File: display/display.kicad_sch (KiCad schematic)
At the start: 14 parts, among them J1 DIN41612_03x32_ABC

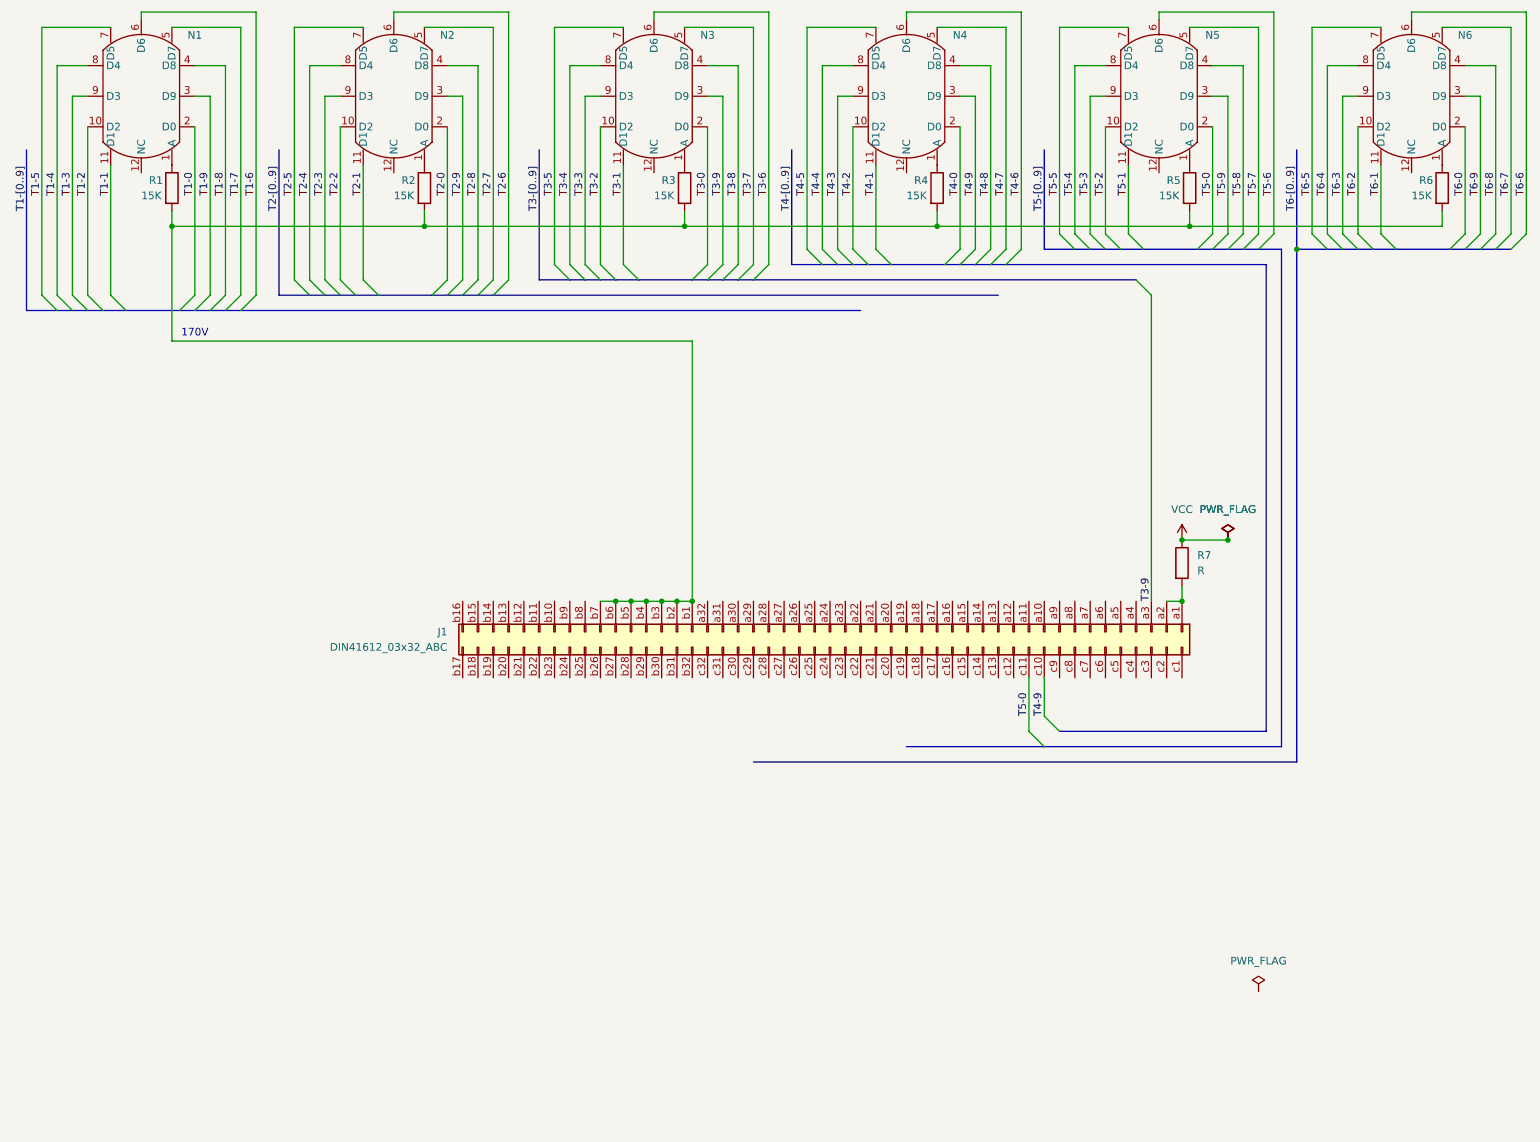
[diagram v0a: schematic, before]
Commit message: Complete rev 1 (alpha) schematics. Both pass DRC.
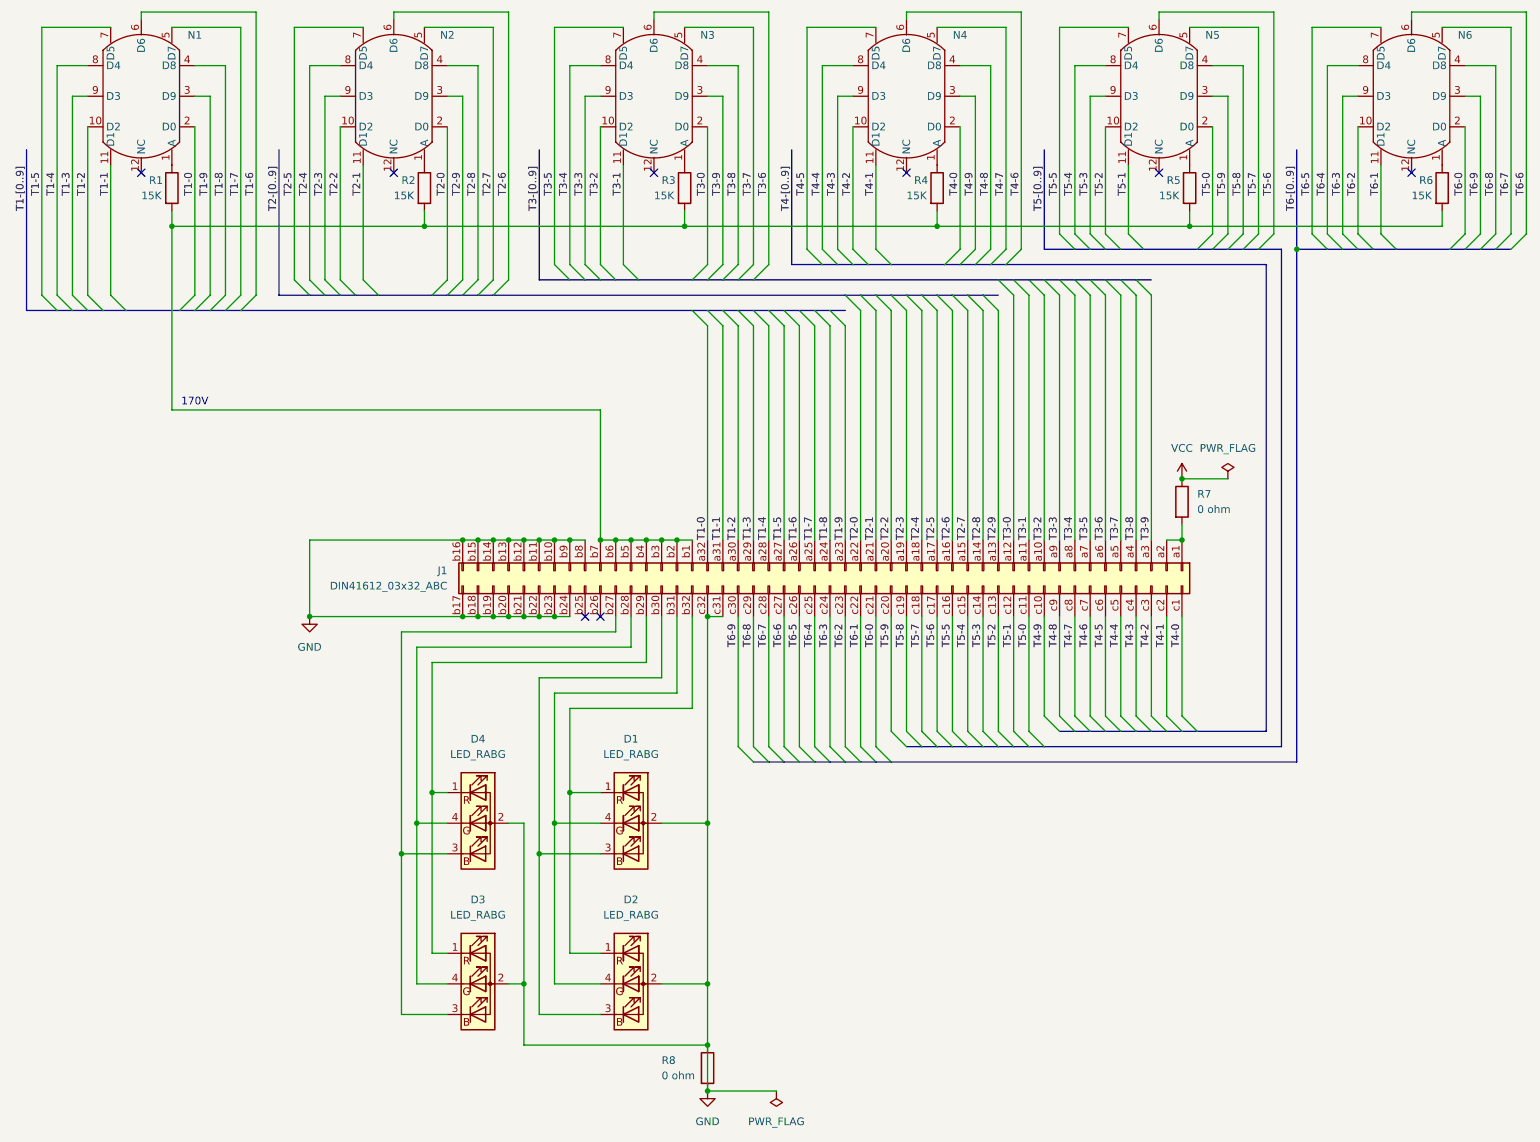
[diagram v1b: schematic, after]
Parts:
- added D1, D2, D3, D4: LED_RABG, symbol Device:LED_RABG
- added R8: 0 ohm, symbol Device:R
- R7: value R -> 0 ohm
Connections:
- net T1-0: now also J1.a32 (Pin_a32)
- net T1-1: now also J1.a31 (Pin_a31)
- net T1-2: now also J1.a30 (Pin_a30)
- net T1-3: now also J1.a29 (Pin_a29)
- net T1-4: now also J1.a28 (Pin_a28)
- net T1-5: now also J1.a27 (Pin_a27)
- net T1-6: now also J1.a26 (Pin_a26)
- net T1-7: now also J1.a25 (Pin_a25)
- net T1-8: now also J1.a24 (Pin_a24)
- net T1-9: now also J1.a23 (Pin_a23)
- net T2-0: now also J1.a22 (Pin_a22)
- net T2-1: now also J1.a21 (Pin_a21)
- net T2-2: now also J1.a20 (Pin_a20)
- net T2-3: now also J1.a19 (Pin_a19)
- net T2-4: now also J1.a18 (Pin_a18)
- net T2-5: now also J1.a17 (Pin_a17)
- net T2-6: now also J1.a16 (Pin_a16)
- net T2-7: now also J1.a15 (Pin_a15)
- net T2-8: now also J1.a14 (Pin_a14)
- net T2-9: now also J1.a13 (Pin_a13)
- net T3-0: now also J1.a12 (Pin_a12)
- net T3-1: now also J1.a11 (Pin_a11)
- net T3-2: now also J1.a10 (Pin_a10)
- net T3-3: now also J1.a9 (Pin_a9)
- net T3-4: now also J1.a8 (Pin_a8)
- net T3-5: now also J1.a7 (Pin_a7)
- net T3-6: now also J1.a6 (Pin_a6)
- net T3-7: now also J1.a5 (Pin_a5)
- net T3-8: now also J1.a4 (Pin_a4)
- net T4-0: now also J1.c1 (Pin_c1)
- net T4-1: now also J1.c2 (Pin_c2)
- net T4-2: now also J1.c3 (Pin_c3)
- net T4-3: now also J1.c4 (Pin_c4)
- net T4-4: now also J1.c5 (Pin_c5)
- net T4-5: now also J1.c6 (Pin_c6)
- net T4-6: now also J1.c7 (Pin_c7)
- net T4-7: now also J1.c8 (Pin_c8)
- net T4-8: now also J1.c9 (Pin_c9)
- net T5-1: now also J1.c12 (Pin_c12)
- net T5-2: now also J1.c13 (Pin_c13)
- net T5-3: now also J1.c14 (Pin_c14)
- net T5-4: now also J1.c15 (Pin_c15)
- net T5-5: now also J1.c16 (Pin_c16)
- net T5-6: now also J1.c17 (Pin_c17)
- net T5-7: now also J1.c18 (Pin_c18)
- net T5-8: now also J1.c19 (Pin_c19)
- net T5-9: now also J1.c20 (Pin_c20)
- net T6-0: now also J1.c21 (Pin_c21)
- net T6-1: now also J1.c22 (Pin_c22)
- net T6-2: now also J1.c23 (Pin_c23)
- net T6-3: now also J1.c24 (Pin_c24)
- net T6-4: now also J1.c25 (Pin_c25)
- net T6-5: now also J1.c26 (Pin_c26)
- net T6-6: now also J1.c27 (Pin_c27)
- net T6-7: now also J1.c28 (Pin_c28)
- net T6-8: now also J1.c29 (Pin_c29)
- net T6-9: now also J1.c30 (Pin_c30)
- net GND: now reaches J1.b10 (Pin_b10)
- net GND: now also J1.b11 (Pin_b11), J1.b12 (Pin_b12), J1.b13 (Pin_b13), J1.b14 (Pin_b14), J1.b15 (Pin_b15), J1.b16 (Pin_b16), J1.b17 (Pin_b17), J1.b18 (Pin_b18), J1.b19 (Pin_b19), J1.b20 (Pin_b20), J1.b21 (Pin_b21), J1.b22 (Pin_b22), J1.b23 (Pin_b23), J1.b24 (Pin_b24), J1.b8 (Pin_b8), J1.b9 (Pin_b9), J1.c31 (Pin_c31), J1.c32 (Pin_c32), D1.2 (A), D2.2 (A), D3.2 (A), D4.2 (A), R8.1, R8.2
- net at J1.b27 (Pin_b27): now also D3.3 (BK), D4.3 (BK)
- net at J1.b28 (Pin_b28): now also D3.4 (GK), D4.4 (GK)
- net at J1.b29 (Pin_b29): now also D3.1 (RK), D4.1 (RK)
- net at J1.b30 (Pin_b30): now also D1.3 (BK), D2.3 (BK)
- net at J1.b31 (Pin_b31): now also D1.4 (GK), D2.4 (GK)
- net at J1.b32 (Pin_b32): now also D1.1 (RK), D2.1 (RK)
- no-connect marks 0 -> 8
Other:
- moved on the sheet: J1, R7

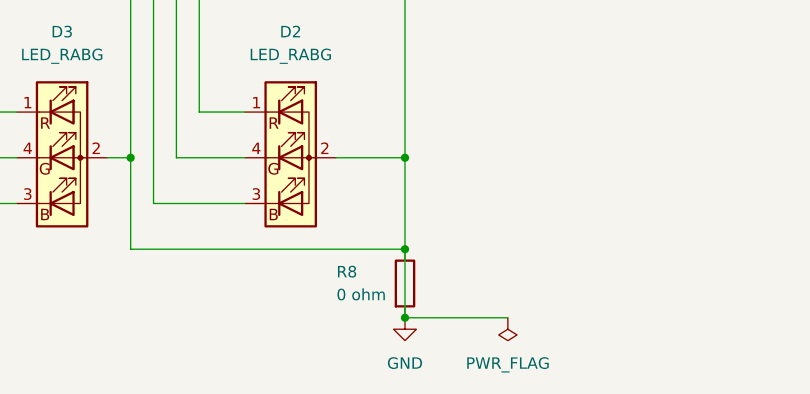
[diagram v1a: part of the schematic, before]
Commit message: Assign footprints for display and create PCB design
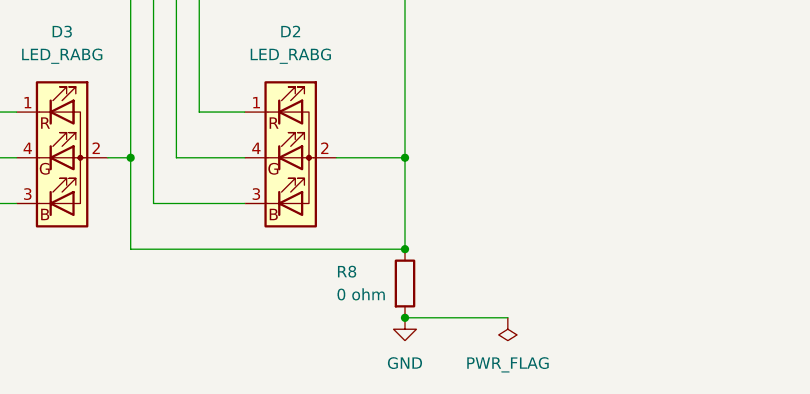
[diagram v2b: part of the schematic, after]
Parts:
- D1, D2, D3, D4: footprint (none) -> LED_THT:LED_D5.0mm-4_RGB
- J1: footprint (none) -> Connector_DIN:DIN41612_R_3x32_Female_Horizontal_THT
- N1, N2, N3, N4, N5, N6: footprint (none) -> hatsunearu:IN_12B_Socket
- R1, R2, R3, R4, R5, R6, R7, R8: footprint (none) -> Resistor_THT:R_Box_L14.0mm_W5.0mm_P9.00mm
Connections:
- net GND: no longer D1.2 (A), D2.2 (A), D3.2 (A), D4.2 (A), J1.c31 (Pin_c31), J1.c32 (Pin_c32), R8.1
- new net: D1.2 (A), D2.2 (A), D3.2 (A), D4.2 (A), J1.c31 (Pin_c31), J1.c32 (Pin_c32), R8.1
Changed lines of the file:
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@@
 		)
 	)
-	(wire
-		(pts
-			(xy 129.54 196.85) (xy 129.54 189.23)
-		)
-		(stroke
-			(width 0)
-			(type default)
-		)
-	)
 	(bus
 		(pts
@@
 			)
 		)
-		(property "Footprint" ""
+		(property "Footprint" "hatsunearu:IN_12B_Socket"
 			(at 246.38 31.75 0)
 			(effects
@@
 			)
 		)
-		(property "Footprint" ""
+		(property "Footprint" "hatsunearu:IN_12B_Socket"
 			(at 162.56 31.75 0)
 			(effects
@@
 			)
 		)
-		(property "Footprint" ""
+		(property "Footprint" "Resistor_THT:R_Box_L14.0mm_W5.0mm_P9.00mm"
 			(at 165.862 46.99 90)
 			(effects
@@
 			)
 		)
-		(property "Footprint" ""
+		(property "Footprint" "Connector_DIN:DIN41612_R_3x32_Female_Horizontal_THT"
 			(at 170.18 110.49 0)
 			(effects
@@
 			)
 		)
-		(property "Footprint" ""
+		(property "Footprint" "Resistor_THT:R_Box_L14.0mm_W5.0mm_P9.00mm"
 			(at 206.502 99.06 90)
 			(effects
@@
 			)
 		)
-		(property "Footprint" ""
+		(property "Footprint" "LED_THT:LED_D5.0mm-4_RGB"
 			(at 91.44 153.67 0)
 			(effects
@@
 			)
 		)
-		(property "Footprint" ""
+		(property "Footprint" "Resistor_THT:R_Box_L14.0mm_W5.0mm_P9.00mm"
 			(at 123.952 46.99 90)
 			(effects
@@
 			)
 		)
-		(property "Footprint" ""
+		(property "Footprint" "Resistor_THT:R_Box_L14.0mm_W5.0mm_P9.00mm"
 			(at 38.862 46.99 90)
 			(effects
@@
 			)
 		)
-		(property "Footprint" ""
+		(property "Footprint" "Resistor_THT:R_Box_L14.0mm_W5.0mm_P9.00mm"
 			(at 207.772 46.99 90)
 			(effects
@@
 			)
 		)
-		(property "Footprint" ""
+		(property "Footprint" "LED_THT:LED_D5.0mm-4_RGB"
 			(at 116.84 180.34 0)
 			(effects
@@
 			)
 		)
-		(property "Footprint" ""
+		(property "Footprint" "Resistor_THT:R_Box_L14.0mm_W5.0mm_P9.00mm"
 			(at 127.762 193.04 90)
 			(effects
@@
 			)
 		)
-		(property "Footprint" ""
+		(property "Footprint" "hatsunearu:IN_12B_Socket"
 			(at 77.47 31.75 0)
 			(effects
@@
 			)
 		)
-		(property "Footprint" ""
+		(property "Footprint" "hatsunearu:IN_12B_Socket"
 			(at 35.56 31.75 0)
 			(effects
@@
 			)
 		)
-		(property "Footprint" ""
+		(property "Footprint" "hatsunearu:IN_12B_Socket"
 			(at 120.65 31.75 0)
 			(effects
@@
 			)
 		)
-		(property "Footprint" ""
+		(property "Footprint" "LED_THT:LED_D5.0mm-4_RGB"
 			(at 116.84 153.67 0)
 			(effects
@@
 			)
 		)
-		(property "Footprint" ""
+		(property "Footprint" "Resistor_THT:R_Box_L14.0mm_W5.0mm_P9.00mm"
 			(at 80.772 46.99 90)
 			(effects
@@
 			)
 		)
-		(property "Footprint" ""
+		(property "Footprint" "LED_THT:LED_D5.0mm-4_RGB"
 			(at 91.44 180.34 0)
 			(effects
@@
 			)
 		)
-		(property "Footprint" ""
+		(property "Footprint" "Resistor_THT:R_Box_L14.0mm_W5.0mm_P9.00mm"
 			(at 249.682 46.99 90)
 			(effects
@@
 			)
 		)
-		(property "Footprint" ""
+		(property "Footprint" "hatsunearu:IN_12B_Socket"
 			(at 204.47 31.75 0)
 			(effects

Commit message: Layout is ongoing
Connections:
- net T4-0: now also J1.c30 (Pin_c30); no longer J1.c1 (Pin_c1)
- net T4-1: now also J1.c29 (Pin_c29); no longer J1.c2 (Pin_c2)
- net T4-2: now also J1.c28 (Pin_c28); no longer J1.c3 (Pin_c3)
- net T4-3: now also J1.c27 (Pin_c27); no longer J1.c4 (Pin_c4)
- net T4-4: now also J1.c26 (Pin_c26); no longer J1.c5 (Pin_c5)
- net T4-5: now also J1.c25 (Pin_c25); no longer J1.c6 (Pin_c6)
- net T4-6: now also J1.c24 (Pin_c24); no longer J1.c7 (Pin_c7)
- net T4-7: now also J1.c23 (Pin_c23); no longer J1.c8 (Pin_c8)
- net T4-8: now also J1.c22 (Pin_c22); no longer J1.c9 (Pin_c9)
- net T4-9: now also J1.c21 (Pin_c21); no longer J1.c10 (Pin_c10)
- net T5-0: now also J1.c20 (Pin_c20); no longer J1.c11 (Pin_c11)
- net T5-1: now also J1.c19 (Pin_c19); no longer J1.c12 (Pin_c12)
- net T5-2: now also J1.c18 (Pin_c18); no longer J1.c13 (Pin_c13)
- net T5-3: now also J1.c17 (Pin_c17); no longer J1.c14 (Pin_c14)
- net T5-4: now also J1.c16 (Pin_c16); no longer J1.c15 (Pin_c15)
- net T5-5: now also J1.c15 (Pin_c15); no longer J1.c16 (Pin_c16)
- net T5-6: now also J1.c14 (Pin_c14); no longer J1.c17 (Pin_c17)
- net T5-7: now also J1.c13 (Pin_c13); no longer J1.c18 (Pin_c18)
- net T5-8: now also J1.c12 (Pin_c12); no longer J1.c19 (Pin_c19)
- net T5-9: now also J1.c11 (Pin_c11); no longer J1.c20 (Pin_c20)
- net T6-0: now also J1.c5 (Pin_c5); no longer J1.c21 (Pin_c21)
- net T6-1: now also J1.c6 (Pin_c6); no longer J1.c22 (Pin_c22)
- net T6-2: now also J1.c7 (Pin_c7); no longer J1.c23 (Pin_c23)
- net T6-3: now also J1.c8 (Pin_c8); no longer J1.c24 (Pin_c24)
- net T6-4: now also J1.c9 (Pin_c9); no longer J1.c25 (Pin_c25)
- net T6-5: now also J1.c10 (Pin_c10); no longer J1.c26 (Pin_c26)
- net T6-6: now also J1.c1 (Pin_c1); no longer J1.c27 (Pin_c27)
- net T6-7: now also J1.c2 (Pin_c2); no longer J1.c28 (Pin_c28)
- net T6-8: now also J1.c3 (Pin_c3); no longer J1.c29 (Pin_c29)
- net T6-9: now also J1.c4 (Pin_c4); no longer J1.c30 (Pin_c30)
